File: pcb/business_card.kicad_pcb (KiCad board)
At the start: 2 copper layers, 88.9 x 50.8 mm, 71 parts, among them J3 USB_A, J4 Conn_ARM_SWD_TagConnect_TC2030, SW1 SW_SPST, U1 MIC5504-3.3YM5, U2 STM32G030F6P6

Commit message: add updates
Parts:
- J4: moved to B.Cu
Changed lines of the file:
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@@
-    )
-  )
-  (footprint "Connector:Tag-Connect_TC2030-IDC-NL_2x03_P1.27mm_Vertical" (layer "F.Cu")
-    (at 127.985796 121.746296 90)
-    (descr "Tag-Connect programming header; http://www.tag-connect.com/Materials/TC2030-IDC-NL.pdf")
-    (tags "tag connect programming header pogo pins")
-    (property "Sheetfile" "business_card_v1.kicad_sch")
-    (property "Sheetname" "")
-    (property "exclude_from_bom" "")
-    (property "ki_description" "Tag-Connect ARM Cortex SWD JTAG connector, 6 pin")
-    (property "ki_keywords" "Cortex Debug Connector ARM SWD JTAG")
-    (attr exclude_from_pos_files exclude_from_bom)
-    (fp_text reference "J4" (at 0 2.7 90) (layer "F.SilkS") hide
-        (effects (font (size 1 1) (thickness 0.15)))
-    )
-    (fp_text value "Conn_ARM_SWD_TagConnect_TC2030" (at 0 -2.3 90) (layer "F.Fab") hide
-        (effects (font (size 1 1) (thickness 0.15)))
-    )
-    (fp_text user "KEEPOUT" (at 0 0 90) (layer "Cmts.User") hide
-        (effects (font (size 0.4 0.4) (thickness 0.07)))
-    )
-    (fp_text user "${REFERENCE}" (at 0 0 90) (layer "F.Fab")
-        (effects (font (size 1 1) (thickness 0.15)))
-    )
-    (fp_line (start -1.905 1.27) (end -1.905 0.635)
-      (stroke (width 0.12) (type solid)) (layer "F.SilkS"))
-    (fp_line (start -1.27 1.27) (end -1.905 1.27)
-      (stroke (width 0.12) (type solid)) (layer "F.SilkS"))
-    (fp_line (start -3.5 -2) (end 3.5 -2)
-      (stroke (width 0.05) (type solid)) (layer "F.CrtYd"))
-    (fp_line (start -3.5 2) (end -3.5 -2)
-      (stroke (width 0.05) (type solid)) (layer "F.CrtYd"))
-    (fp_line (start 3.5 -2) (end 3.5 2)
-      (stroke (width 0.05) (type solid)) (layer "F.CrtYd"))
-    (fp_line (start 3.5 2) (end -3.5 2)
-      (stroke (width 0.05) (type solid)) (layer "F.CrtYd"))
-    (pad "" np_thru_hole circle (at -2.54 0 90) (size 0.9906 0.9906) (drill 0.9906) (layers "*.Cu" "*.Mask"))
-    (pad "" np_thru_hole circle (at 2.54 -1.016 90) (size 0.9906 0.9906) (drill 0.9906) (layers "*.Cu" "*.Mask"))
-    (pad "" np_thru_hole circle (at 2.54 1.016 90) (size 0.9906 0.9906) (drill 0.9906) (layers "*.Cu" "*.Mask"))
-    (pad "1" connect circle (at -1.27 0.635 90) (size 0.7874 0.7874) (layers "F.Cu" "F.Mask")
-      (net 6 "+3V3") (pinfunction "VCC") (pintype "power_in"))
-    (pad "2" connect circle (at -1.27 -0.635 90) (size 0.7874 0.7874) (layers "F.Cu" "F.Mask")
-      (net 7 "SWDIO") (pinfunction "SWDIO") (pintype "bidirectional"))
-    (pad "3" connect circle (at 0 0.635 90) (size 0.7874 0.7874) (layers "F.Cu" "F.Mask")
-      (net 2 "~{RST}") (pinfunction "~{RESET}") (pintype "open_collector"))
-    (pad "4" connect circle (at 0 -0.635 90) (size 0.7874 0.7874) (layers "F.Cu" "F.Mask")
-      (net 3 "SWDCLK") (pinfunction "SWCLK") (pintype "output"))
-    (pad "5" connect circle (at 1.27 0.635 90) (size 0.7874 0.7874) (layers "F.Cu" "F.Mask")
-      (net 1 "GND") (pinfunction "GND") (pintype "power_in"))
-    (pad "6" connect circle (at 1.27 -0.635 90) (size 0.7874 0.7874) (layers "F.Cu" "F.Mask")
-      (net 4 "unconnected-(J4-SWO-Pad6)") (pinfunction "SWO") (pintype "input+no_connect"))
-    (zone (net 0) (net_name "") (layer "F.Cu") (hatch full 0.508)
-      (connect_pads (clearance 0))
-      (min_thickness 0.254) (filled_areas_thickness no)
-      (keepout (tracks allowed) (vias not_allowed) (pads allowed) (copperpour not_allowed) (footprints not_allowed))
-      (fill (thermal_gap 0.508) (thermal_bridge_width 0.508))
-      (polygon
-        (pts
-          (xy 127.350796 120.476296)
-          (xy 127.350796 123.016296)
-          (xy 128.620796 123.016296)
-          (xy 128.620796 120.476296)
-        )
-      )
     )
   )
@@
     )
   )
+  (footprint "Connector:Tag-Connect_TC2030-IDC-NL_2x03_P1.27mm_Vertical" (layer "B.Cu")
+    (at 127.985796 121.746296 90)
+    (descr "Tag-Connect programming header; http://www.tag-connect.com/Materials/TC2030-IDC-NL.pdf")
+    (tags "tag connect programming header pogo pins")
+    (property "Sheetfile" "business_card_v1.kicad_sch")
+    (property "Sheetname" "")
+    (property "exclude_from_bom" "")
+    (property "ki_description" "Tag-Connect ARM Cortex SWD JTAG connector, 6 pin")
+    (property "ki_keywords" "Cortex Debug Connector ARM SWD JTAG")
+    (attr exclude_from_pos_files exclude_from_bom)
+    (fp_text reference "J4" (at 0 -2.7 90) (layer "B.SilkS") hide
+        (effects (font (size 1 1) (thickness 0.15)) (justify mirror))
+    )
+    (fp_text value "Conn_ARM_SWD_TagConnect_TC2030" (at 0 2.3 90) (layer "B.Fab") hide
+        (effects (font (size 1 1) (thickness 0.15)) (justify mirror))
+    )
+    (fp_text user "KEEPOUT" (at 0 0 90) (layer "Cmts.User") hide
+        (effects (font (size 0.4 0.4) (thickness 0.07)))
+    )
+    (fp_text user "${REFERENCE}" (at 0 0 90) (layer "B.Fab")
+        (effects (font (size 1 1) (thickness 0.15)) (justify mirror))
+    )
+    (fp_line (start -1.905 -1.27) (end -1.905 -0.635)
+      (stroke (width 0.12) (type solid)) (layer "B.SilkS"))
+    (fp_line (start -1.27 -1.27) (end -1.905 -1.27)
+      (stroke (width 0.12) (type solid)) (layer "B.SilkS"))
+    (fp_line (start -3.5 -2) (end -3.5 2)
+      (stroke (width 0.05) (type solid)) (layer "B.CrtYd"))
+    (fp_line (start -3.5 2) (end 3.5 2)
+      (stroke (width 0.05) (type solid)) (layer "B.CrtYd"))
+    (fp_line (start 3.5 -2) (end -3.5 -2)
+      (stroke (width 0.05) (type solid)) (layer "B.CrtYd"))
+    (fp_line (start 3.5 2) (end 3.5 -2)
+      (stroke (width 0.05) (type solid)) (layer "B.CrtYd"))
+    (pad "" np_thru_hole circle (at -2.54 0 90) (size 0.9906 0.9906) (drill 0.9906) (layers "*.Cu" "*.Mask"))
+    (pad "" np_thru_hole circle (at 2.54 -1.016 90) (size 0.9906 0.9906) (drill 0.9906) (layers "*.Cu" "*.Mask"))
+    (pad "" np_thru_hole circle (at 2.54 1.016 90) (size 0.9906 0.9906) (drill 0.9906) (layers "*.Cu" "*.Mask"))
+    (pad "1" connect circle (at -1.27 -0.635 90) (size 0.7874 0.7874) (layers "B.Cu" "B.Mask")
+      (net 6 "+3V3") (pinfunction "VCC") (pintype "power_in"))
+    (pad "2" connect circle (at -1.27 0.635 90) (size 0.7874 0.7874) (layers "B.Cu" "B.Mask")
+      (net 7 "SWDIO") (pinfunction "SWDIO") (pintype "bidirectional"))
+    (pad "3" connect circle (at 0 -0.635 90) (size 0.7874 0.7874) (layers "B.Cu" "B.Mask")
+      (net 2 "~{RST}") (pinfunction "~{RESET}") (pintype "open_collector"))
+    (pad "4" connect circle (at 0 0.635 90) (size 0.7874 0.7874) (layers "B.Cu" "B.Mask")
+      (net 3 "SWDCLK") (pinfunction "SWCLK") (pintype "output"))
+    (pad "5" connect circle (at 1.27 -0.635 90) (size 0.7874 0.7874) (layers "B.Cu" "B.Mask")
+      (net 1 "GND") (pinfunction "GND") (pintype "power_in"))
+    (pad "6" connect circle (at 1.27 0.635 90) (size 0.7874 0.7874) (layers "B.Cu" "B.Mask")
+      (net 4 "unconnected-(J4-SWO-Pad6)") (pinfunction "SWO") (pintype "input+no_connect"))
+    (zone (net 0) (net_name "") (layer "B.Cu") (hatch full 0.508)
+      (connect_pads (clearance 0))
+      (min_thickness 0.254) (filled_areas_thickness no)
+      (keepout (tracks allowed) (vias not_allowed) (pads allowed) (copperpour not_allowed) (footprints not_allowed))
+      (fill (thermal_gap 0.508) (thermal_bridge_width 0.508))
+      (polygon
+        (pts
+          (xy 128.620796 120.476296)
+          (xy 128.620796 123.016296)
+          (xy 127.350796 123.016296)
+          (xy 127.350796 120.476296)
+        )
+      )
+    )
+  )

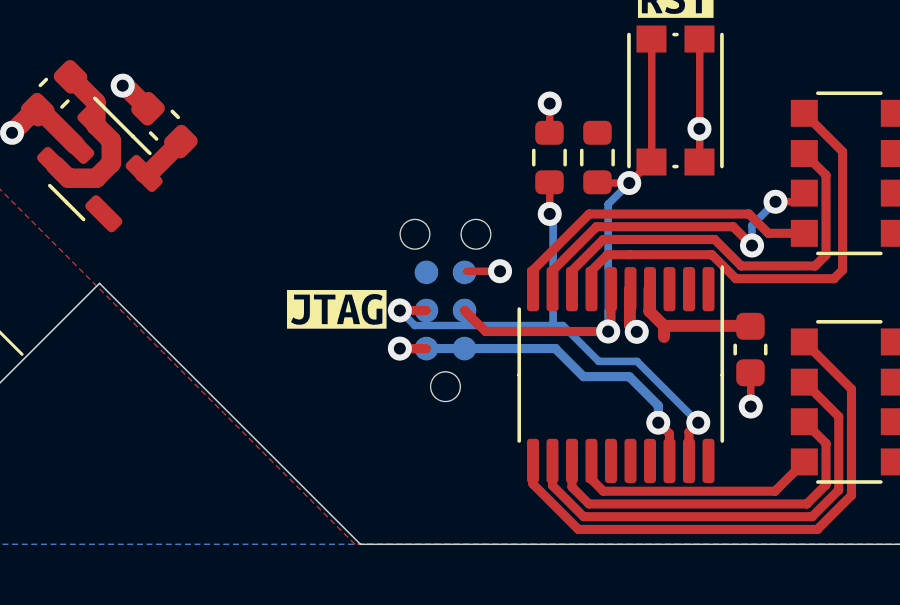
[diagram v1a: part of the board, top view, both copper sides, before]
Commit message: use leds instead, add bom, update code
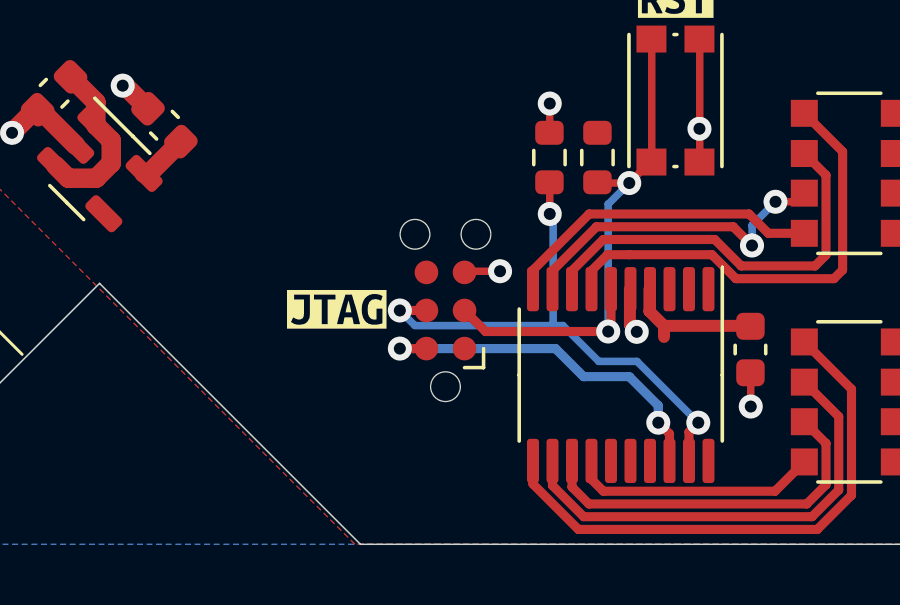
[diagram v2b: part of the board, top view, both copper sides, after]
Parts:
- D1, D10, D11, D12, D13, D14, D15, D16, D17, D18, D19, D2, D20, D21, D22, D23, D24, D25, D26, D27, D28, D29, D3, D30, D31, D32, D33, D34, D35, D36, D37, D38, D39, D4, D40, D41, D42, D43, D44, D45, D46, D47, D48, D49, D5, D50, D51, D52, D53, D54, D6, D7, D8, D9, LED1, LED2: footprint Diode_SMD:D_0805_2012Metric -> LED_SMD:LED_0805_2012Metric
- J4: moved to F.Cu
